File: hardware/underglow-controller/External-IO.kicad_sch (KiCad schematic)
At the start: 43 parts, among them Q601 STS8DNF3LL, Q602 STS8DNF3LL, Q603 STS8DNF3LL, Q604 MBT3904DW1T1G, Q605 MBT3904DW1T1G, U601 A6213-1, U602 A6213-1

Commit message: Bom fillout + wiring
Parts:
- C602, C607: MPN (none) -> C3216X7R1V475K160AB
- C603, C604, C608, C609: MPN (none) -> 06035C104KAT4A
- R601, R604: MPN (none) -> RMCF0603FT66K5
- R602, R605: MPN (none) -> ERJ-8BWFR068V
- R603, R606: MPN (none) -> RNCP0603FTD10K0
- U601, U602: MPN (none) -> A6213-1
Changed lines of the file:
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@@
+      (effects (font (size 1.27 1.27)) hide)
+    )
+    (property "Description" "RES 66.5K OHM 1% 1/10W 0603" (id 4) (at 81.28 129.54 0)
+      (effects (font (size 1.27 1.27)) hide)
+    )
+    (property "MPN" "RMCF0603FT66K5" (id 5) (at 81.28 129.54 0)
       (effects (font (size 1.27 1.27)) hide)
     )
@@
     )
     (property "Datasheet" "https://www.allegromicro.com/en/products/regulate/led-drivers/led-drivers-for-lighting/a6213" (id 3) (at 99.06 132.08 0)
+      (effects (font (size 1.27 1.27)) hide)
+    )
+    (property "MPN" "A6213-1" (id 4) (at 100.33 132.08 0)
       (effects (font (size 1.27 1.27)) hide)
     )
@@
       (effects (font (size 1.27 1.27)) hide)
     )
+    (property "Description" "RES 0.068 OHM 1% 1W 1206" (id 4) (at 76.2 87.63 0)
+      (effects (font (size 1.27 1.27)) hide)
+    )
+    (property "MPN" "ERJ-8BWFR068V" (id 5) (at 76.2 87.63 0)
+      (effects (font (size 1.27 1.27)) hide)
+    )
     (pin "1")
     (pin "2")
@@
     )
     (property "MPN" "EMVY500ADA470MF80G" (id 4) (at 66.04 48.26 0)
+      (effects (font (size 1.27 1.27)) hide)
+    )
+    (property "Description" "CAP ALUM 47UF 20% 50V SMD" (id 5) (at 66.04 48.26 0)
       (effects (font (size 1.27 1.27)) hide)
     )
@@
       (effects (font (size 1.27 1.27)) hide)
     )
-    (property "MPN" "" (id 4) (at 71.12 124.46 0)
+    (property "MPN" "C3216X7R1V475K160AB" (id 4) (at 71.12 124.46 0)
+      (effects (font (size 1.27 1.27)) hide)
+    )
+    (property "Description" "CAP CER 4.7UF 35V X7R 1206" (id 5) (at 71.12 124.46 0)
       (effects (font (size 1.27 1.27)) hide)
     )
@@
     )
     (property "Datasheet" "~" (id 3) (at 82.55 53.34 0)
+      (effects (font (size 1.27 1.27)) hide)
+    )
+    (property "Description" "RES 66.5K OHM 1% 1/10W 0603" (id 4) (at 82.55 53.34 0)
+      (effects (font (size 1.27 1.27)) hide)
+    )
+    (property "MPN" "RMCF0603FT66K5" (id 5) (at 82.55 53.34 0)
       (effects (font (size 1.27 1.27)) hide)
     )
@@
       (effects (font (size 1.27 1.27)) hide)
     )
+    (property "Description" "CAP CER 0.1UF 50V X7R 0603" (id 4) (at 135.89 127 0)
+      (effects (font (size 1.27 1.27)) hide)
+    )
+    (property "MPN" "06035C104KAT4A" (id 5) (at 135.89 127 0)
+      (effects (font (size 1.27 1.27)) hide)
+    )
     (pin "1")
     (pin "2")
@@
     )
     (property "MPN" "74438356033" (id 4) (at 149.86 48.26 90)
+      (effects (font (size 1.27 1.27)) hide)
+    )
+    (property "Description" "FIXED IND 3.3UH 3.6A 48 MOHM SMD" (id 5) (at 149.86 48.26 0)
       (effects (font (size 1.27 1.27)) hide)
     )
@@
       (effects (font (size 1.27 1.27)) hide)
     )
+    (property "Description" "CAP ALUM 47UF 20% 50V SMD" (id 5) (at 63.5 124.46 0)
+      (effects (font (size 1.27 1.27)) hide)
+    )
     (pin "1")
     (pin "2")
@@
     )
     (property "Datasheet" "~" (id 3) (at 62.23 140.97 0)
+      (effects (font (size 1.27 1.27)) hide)
+    )
+    (property "Description" "RES 10K OHM 1% 1/8W 0603" (id 4) (at 62.23 140.97 0)
+      (effects (font (size 1.27 1.27)) hide)
+    )
+    (property "MPN" "RNCP0603FTD10K0" (id 5) (at 62.23 140.97 0)
       (effects (font (size 1.27 1.27)) hide)
     )
@@
       (effects (font (size 1.27 1.27)) hide)
     )
+    (property "Description" "RES 0.068 OHM 1% 1W 1206" (id 4) (at 74.93 163.83 0)
+      (effects (font (size 1.27 1.27)) hide)
+    )
+    (property "MPN" "ERJ-8BWFR068V" (id 5) (at 74.93 163.83 0)
+      (effects (font (size 1.27 1.27)) hide)
+    )
     (pin "1")
     (pin "2")
@@
       (effects (font (size 1.27 1.27)) hide)
     )
+    (property "Description" "RES 10K OHM 1% 1/8W 0603" (id 4) (at 62.23 66.04 0)
+      (effects (font (size 1.27 1.27)) hide)
+    )
+    (property "MPN" "RNCP0603FTD10K0" (id 5) (at 62.23 66.04 0)
+      (effects (font (size 1.27 1.27)) hide)
+    )
     (pin "1")
     (pin "2")
@@
     )
     (property "Datasheet" "~" (id 3) (at 135.89 50.8 0)
+      (effects (font (size 1.27 1.27)) hide)
+    )
+    (property "Description" "CAP CER 0.1UF 50V X7R 0603" (id 4) (at 135.89 50.8 0)
+      (effects (font (size 1.27 1.27)) hide)
+    )
+    (property "MPN" "06035C104KAT4A" (id 5) (at 135.89 50.8 0)
       (effects (font (size 1.27 1.27)) hide)
     )
@@
       (effects (font (size 1.27 1.27)) hide)
     )
+    (property "Description" "FIXED IND 3.3UH 3.6A 48 MOHM SMD" (id 5) (at 149.86 124.46 0)
+      (effects (font (size 1.27 1.27)) hide)
+    )
     (pin "1")
     (pin "2")
@@
       (effects (font (size 1.27 1.27)) hide)
     )
-    (property "MPN" "" (id 4) (at 72.39 48.26 0)
+    (property "MPN" "C3216X7R1V475K160AB" (id 4) (at 72.39 48.26 0)
+      (effects (font (size 1.27 1.27)) hide)
+    )
+    (property "Description" "CAP CER 4.7UF 35V X7R 1206" (id 5) (at 72.39 48.26 0)
       (effects (font (size 1.27 1.27)) hide)
     )
@@
     )
     (property "Datasheet" "https://www.allegromicro.com/-/media/files/datasheets/a6213-datasheet.pdf" (id 3) (at 100.33 55.88 0)
+      (effects (font (size 1.27 1.27)) hide)
+    )
+    (property "MPN" "A6213-1" (id 4) (at 101.6 55.88 0)
       (effects (font (size 1.27 1.27)) hide)
     )
@@
       (effects (font (size 1.27 1.27)) hide)
     )
+    (property "Description" "CAP CER 0.1UF 50V X7R 0603" (id 4) (at 133.35 59.69 0)
+      (effects (font (size 1.27 1.27)) hide)
+    )
+    (property "MPN" "06035C104KAT4A" (id 5) (at 133.35 59.69 0)
+      (effects (font (size 1.27 1.27)) hide)
+    )
     (pin "1")
     (pin "2")
@@
       (effects (font (size 1.27 1.27)) hide)
     )
+    (property "Description" "CAP CER 0.1UF 50V X7R 0603" (id 4) (at 134.62 135.89 0)
+      (effects (font (size 1.27 1.27)) hide)
+    )
+    (property "MPN" "06035C104KAT4A" (id 5) (at 134.62 135.89 0)
+      (effects (font (size 1.27 1.27)) hide)
+    )

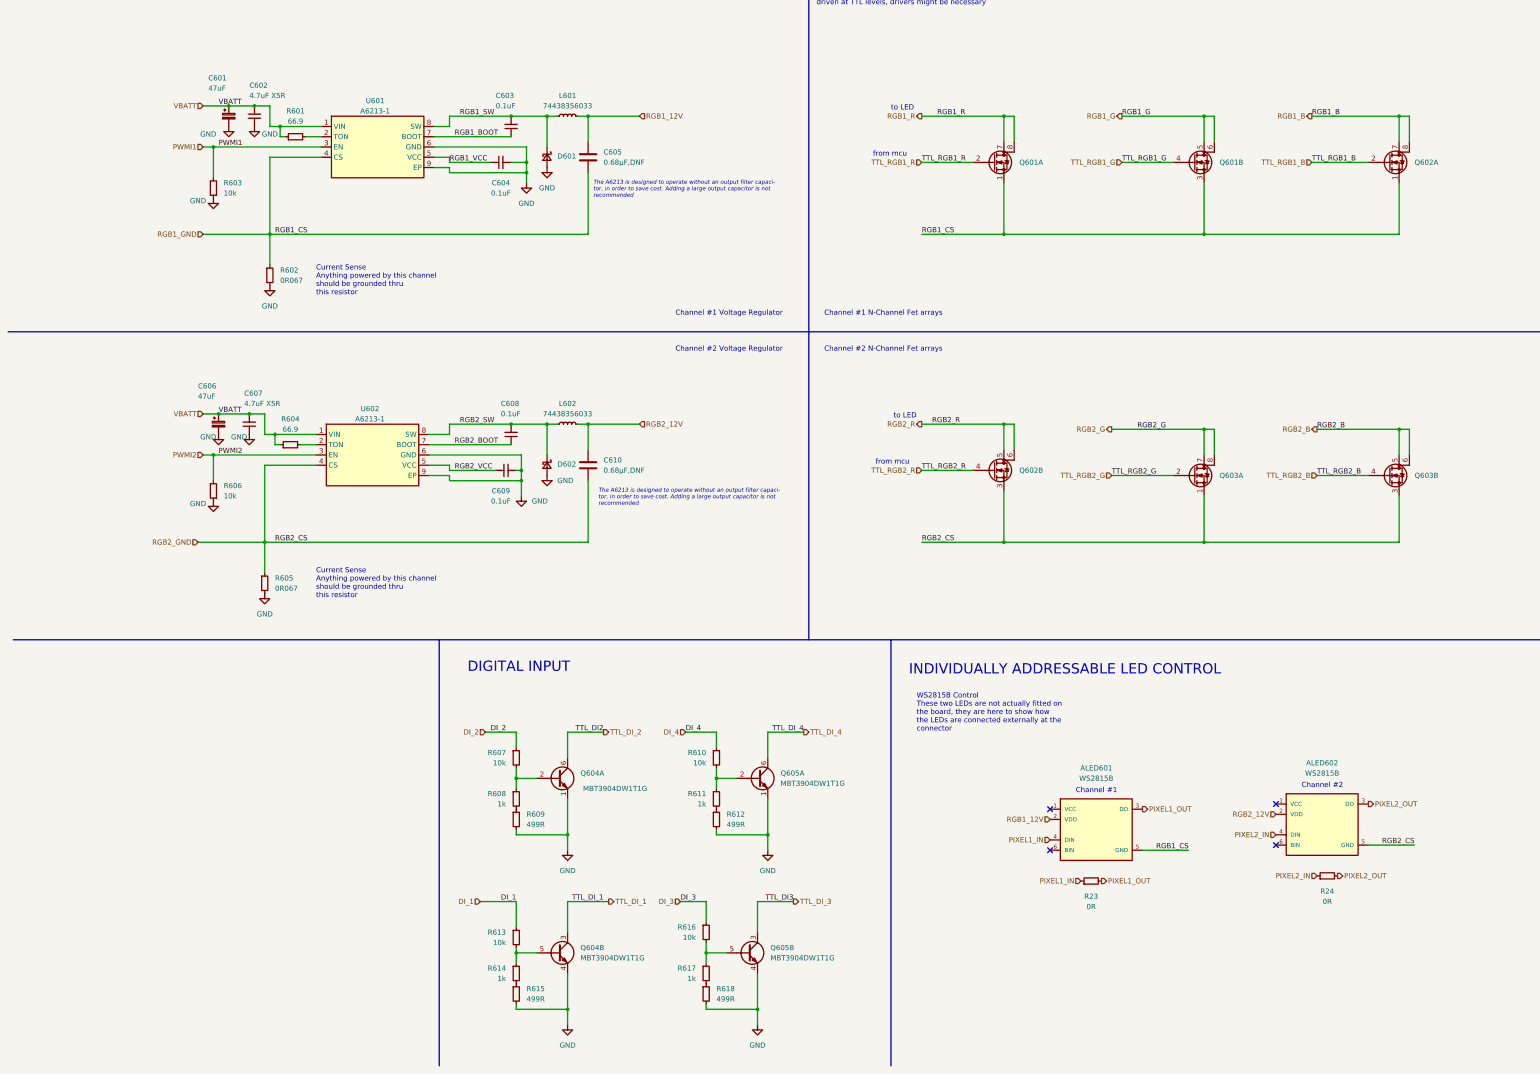
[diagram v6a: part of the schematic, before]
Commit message: hw updates based on prototype issues
* Removes unused hardware and firmware projectes
* Adds some documentation and bom
* cleanup READMEs
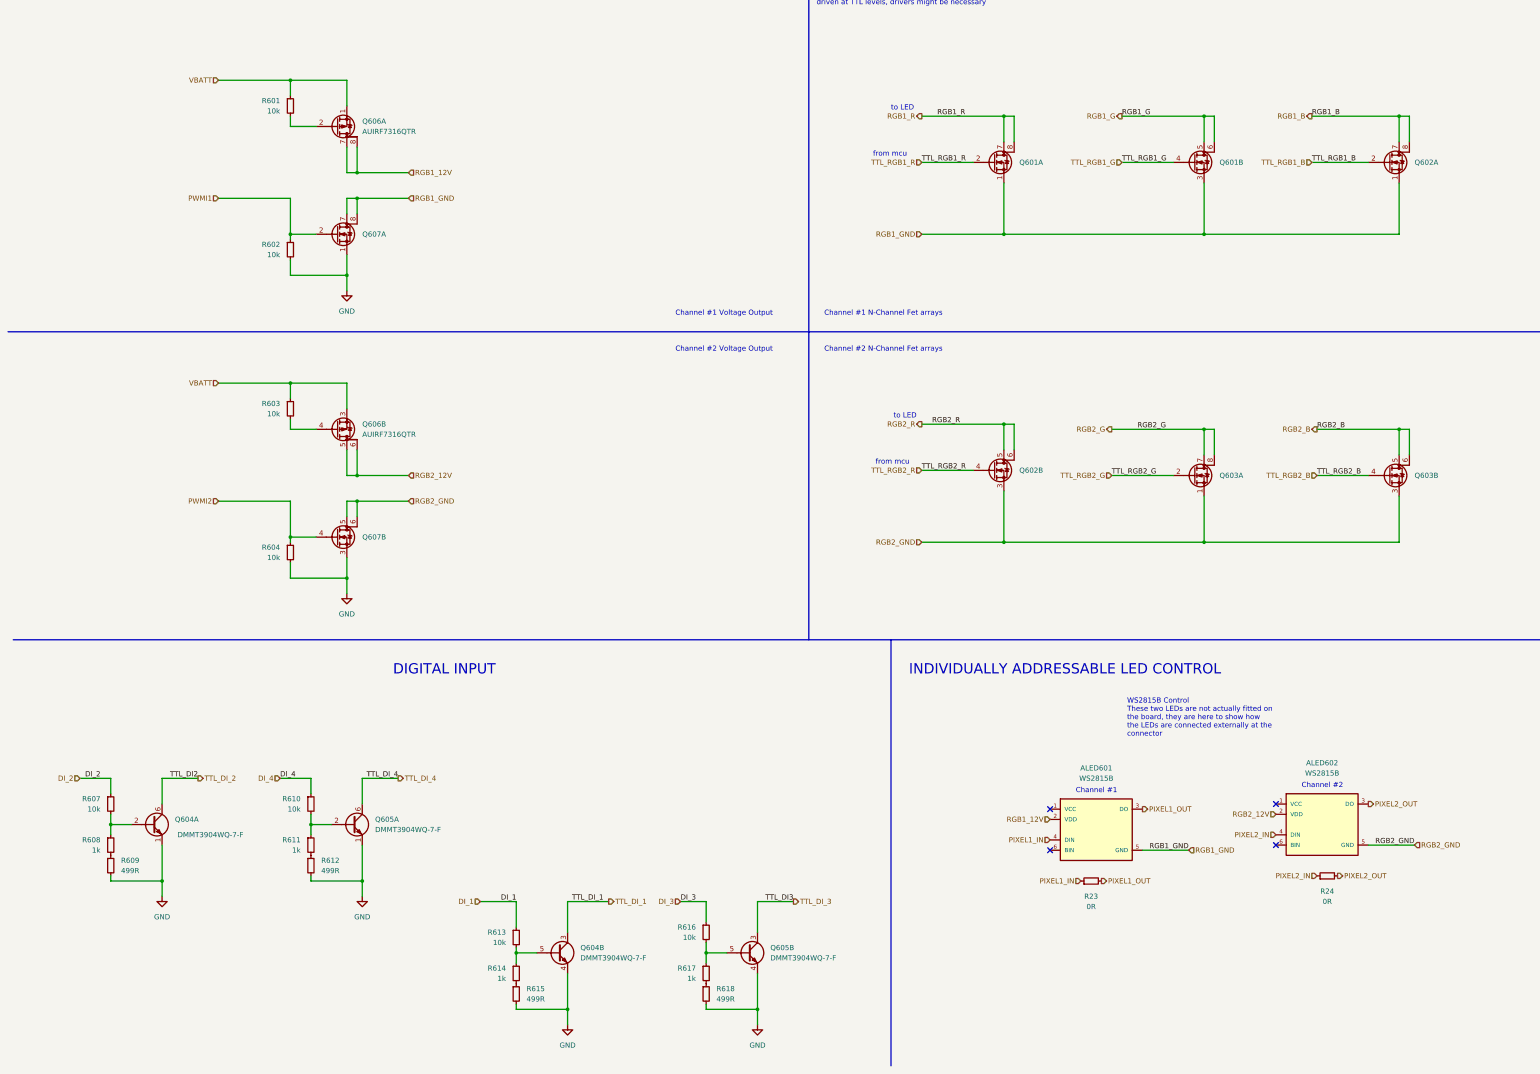
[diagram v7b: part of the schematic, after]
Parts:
- removed C601, C606: 47uF, Capacitor_SMD:CP_Elec_6.3x7.7, symbol Device:C_Polarized_Small
- removed C602, C607: 4.7uF X5R, Capacitor_SMD:C_1206_3216Metric, symbol Device:C_Small
- removed C603, C604, C608, C609: 0.1uF, Capacitor_SMD:C_0603_1608Metric, symbol Device:C_Small
- removed C605, C610: 0.68μF,DNF, Capacitor_SMD:C_1206_3216Metric, symbol Device:C
- removed D601, D602: B250A-13-F, ConeCodes:DIOM5226X240N, symbol Device:D_Schottky_Small
- removed L601, L602: 74438356033, Inductor_SMD:L_Wuerth_MAPI-4030, symbol Device:L_Small
- removed R605: 0R067, Resistor_SMD:R_1206_3216Metric, symbol Device:R_Small
- removed R606: 10k, Resistor_SMD:R_0603_1608Metric, symbol Device:R_Small
- removed U601, U602: A6213-1, Package_SO:SOIC-8-1EP_3.9x4.9mm_P1.27mm_EP2.41x3.3mm_ThermalVias, symbol ConeCodes:A6213-1
- added Q606: AUIRF7316QTR, Package_SO:SO-8_3.9x4.9mm_P1.27mm, symbol Device:Q_Dual_PMOS_S1G1S2G2D2D2D1D1
- added Q607: STS8DNF3LL, Package_SO:SO-8_3.9x4.9mm_P1.27mm, symbol Device:Q_Dual_NMOS_S1G1S2G2D2D2D1D1
- Q604, Q605: value MBT3904DW1T1G -> DMMT3904WQ-7-F; MPN MBT3904DW1T1G -> DMMT3904WQ-7-F
- R601, R604: value 66.9 -> 10k; footprint Resistor_SMD:R_0603_1608Metric -> Resistor_SMD:R_0805_2012Metric; MPN RMCF0603FT66K5 -> RNCP0805FTD10K0
- R602: value 0R067 -> 10k; footprint Resistor_SMD:R_1206_3216Metric -> Resistor_SMD:R_0805_2012Metric; MPN ERJ-8BWFR068V -> RNCP0805FTD10K0
- R603: footprint Resistor_SMD:R_0603_1608Metric -> Resistor_SMD:R_0805_2012Metric; MPN RNCP0603FTD10K0 -> RNCP0805FTD10K0
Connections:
- net GND: now also R604.2, Q607.1 (S), Q607.3 (S); no longer R603.1
- net PWMI1: now also R602.1, Q607.2 (G); no longer R603.2
- net PWMI2: now also R604.1, Q607.4 (G)
- net RGB1_12V: now also Q606.7 (D), Q606.8 (G)
- net RGB1_GND: now also Q607.7 (D), Q607.8 (D); no longer R602.1
- net RGB2_12V: now also Q606.5 (D), Q606.6 (G)
- net RGB2_GND: now also Q607.5 (D), Q607.6 (D)
- net VBATT: now also R603.1, Q606.1 (S), Q606.3 (S); no longer R604.1
- net at R601.2: now also Q606.2 (G)
- new net: Q606.4 (G), R603.2
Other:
- note added: "Channel #1 Voltage Output"
- note added: "Channel #2 Voltage Output"
- note removed: "Channel #1 Voltage Regulator"
- note removed: "Channel #2 Voltage Regulator"
- note removed: "Current Sense Anything powered by this channel should be grounded thru this resistor"
- note removed: "The A6213 is designed to operate without an output filter capaci- tor, in order to save cost. Adding a large output capacitor is not recommended"
- company: cone.codes -> Connor Rigby
- title: CAN RGB Controller V5 -> ${Title}
- moved on the sheet: Q604A, Q605A, R607, R608, R609, R610, R611, R612

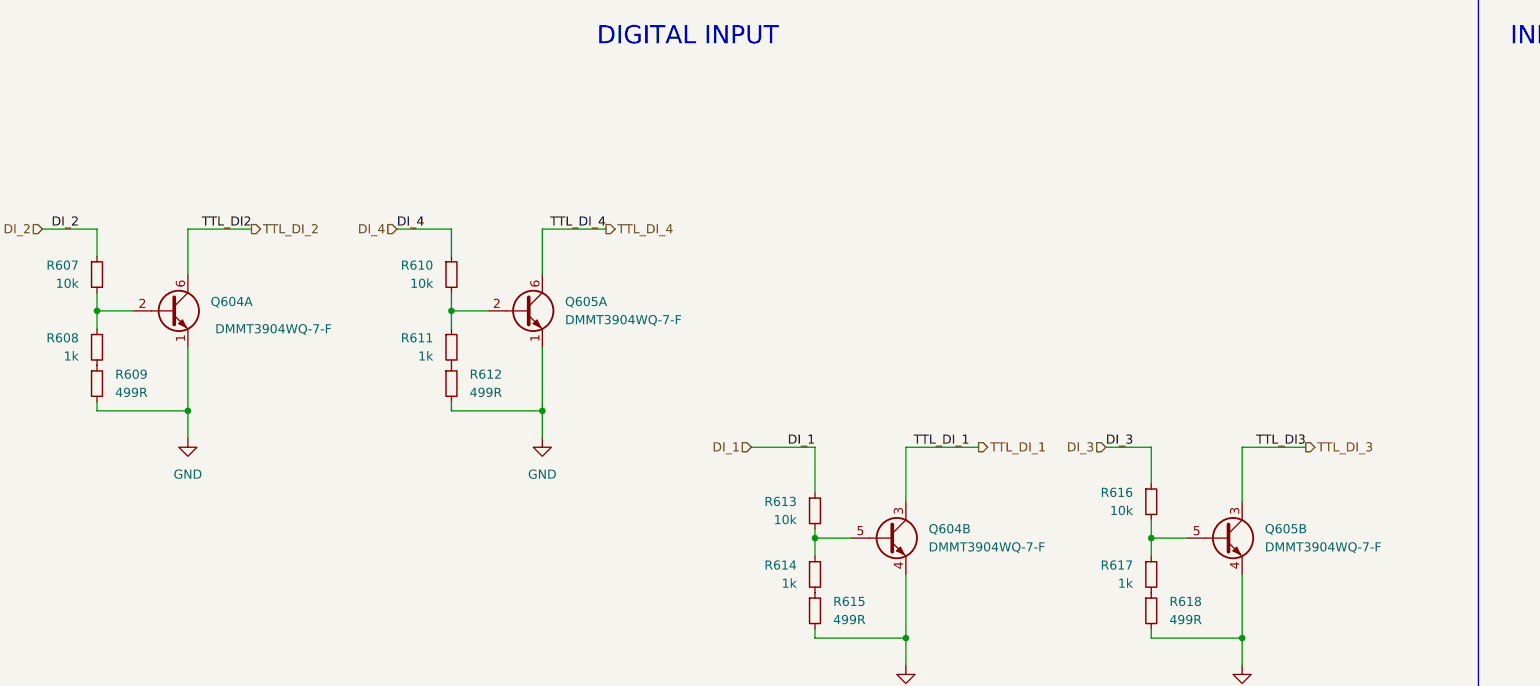
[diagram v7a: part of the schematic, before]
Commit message: hardware updates from board bringup
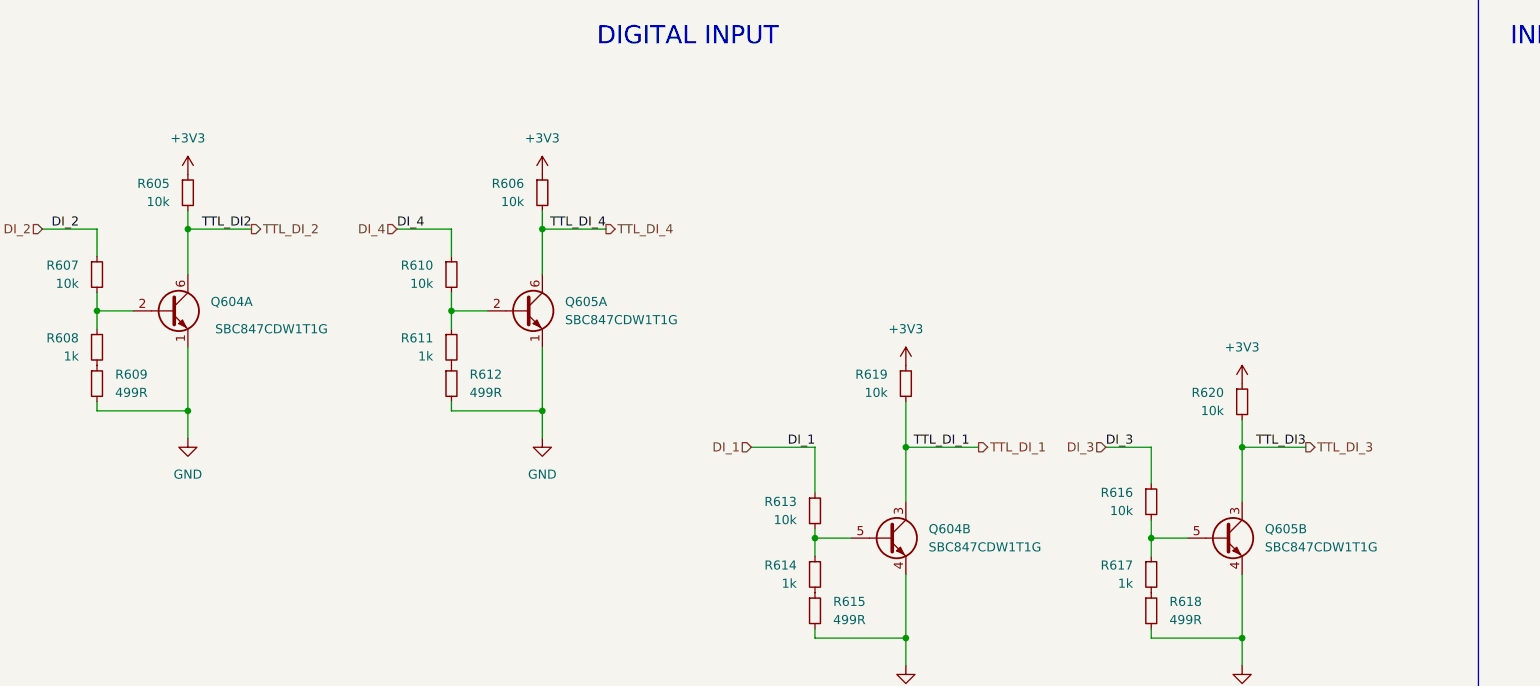
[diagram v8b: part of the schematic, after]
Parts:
- added R605, R606, R619, R620: 10k, Resistor_SMD:R_0402_1005Metric, symbol Device:R_Small
- Q604, Q605: value DMMT3904WQ-7-F -> SBC847CDW1T1G; MPN DMMT3904WQ-7-F -> SBC847CDW1T1G
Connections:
- net TTL_DI_1: now also R619.2
- net TTL_DI_2: now also R605.2
- net TTL_DI_3: now also R620.2
- net TTL_DI_4: now also R606.2
- new net +3V3: R605.1, R606.1, R619.1, R620.1
